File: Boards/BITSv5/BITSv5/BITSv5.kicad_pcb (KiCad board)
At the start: 4 copper layers, 47 x 45 mm, 104 parts, among them J1 Conn_01x10_Pin, J2 USB_C_Receptacle_USB2.0, J3 SOICbite, Q1 Q_NMOS_GSD, SW1 SW_Push, SW3 SLIDE, U1 MCU_RaspberryPi_RP2040_RP2040, U10 USBLC6-2SC6, U11 MS5607-02BA, U2 W25Q128JVS, U3 MAX-M10S, U4 DRF1262TL, U5 LT8653SIV-PBF, U6 TPS2121RUXR, U7 MAX6747KA29+T, U8 LT6703CDC-3, U9 TVS1800DRVR, Y1 12MHz

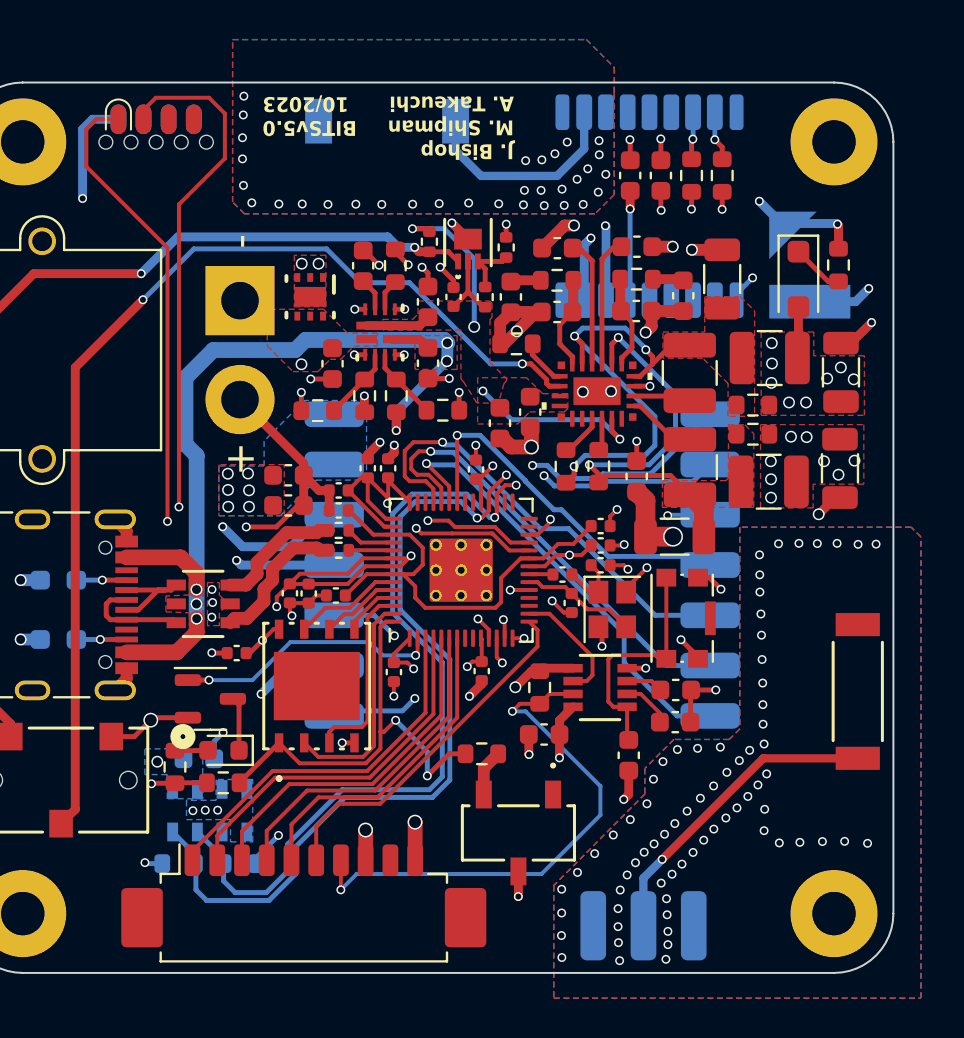
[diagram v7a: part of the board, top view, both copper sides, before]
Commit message: changed BITSv5 antennas to ufl, added TIMEPULSE and EXTINT GPIOs, and exposed GPIO UART over header
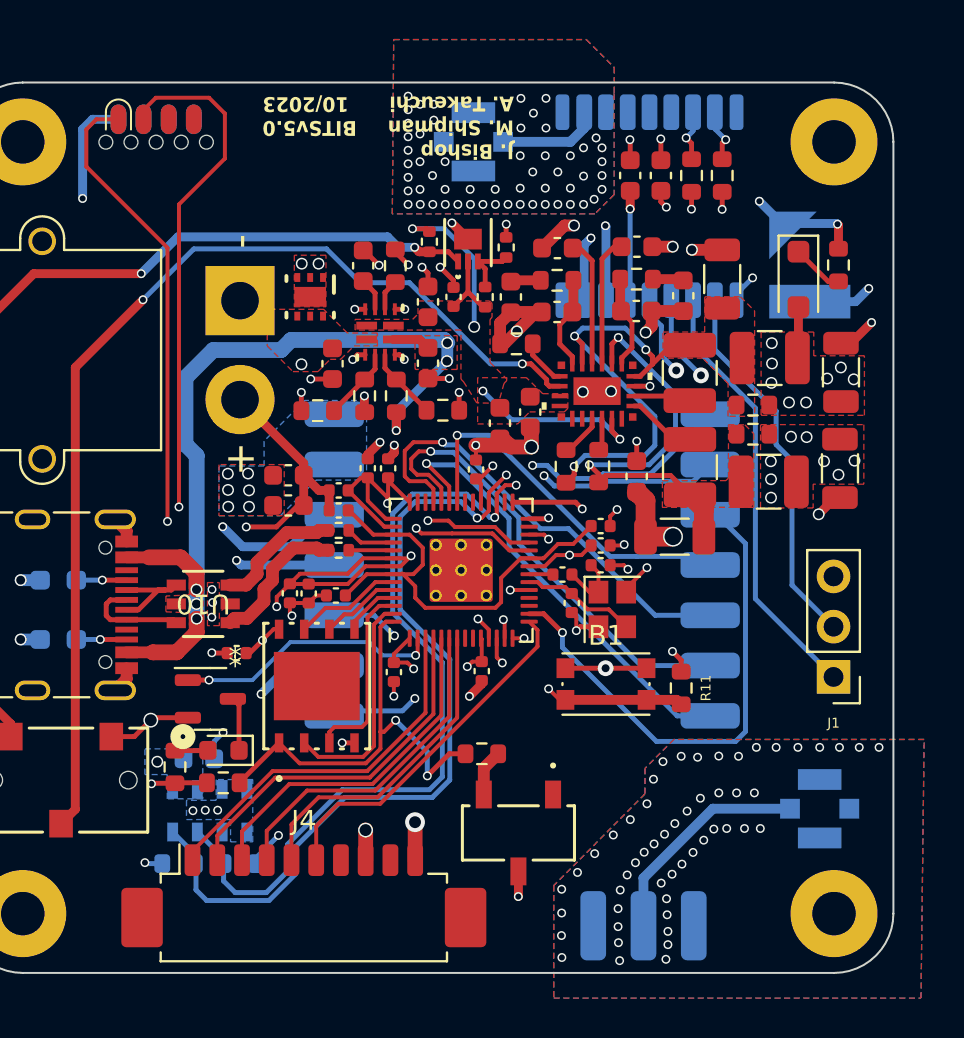
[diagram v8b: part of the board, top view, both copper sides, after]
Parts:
- removed AE1: Antenna, BITSv5:ANT_1575AT_JOT-M
- removed AE2: Antenna, BITSv5:ANT_0915AT43A0026E_JOT
- removed C30, C42: 100nF, Capacitor_SMD:C_0603_1608Metric
- removed C41: 1uF, Capacitor_SMD:C_0603_1608Metric
- removed C43: 200nF, Capacitor_SMD:C_0603_1608Metric
- removed SW1: SW_Push, Button_Switch_SMD:SW_Push_1P1T-SH_NO_CK_KMR2xxG
- removed U7: MAX6747KA29+T, BITSv5:21-0078H_MXM
- added B1: KMR2, Button_Switch_SMD:SW_Push_1P1T_NO_CK_KMR2, F.Cu at (137.7, 72.6)
- added J4: Conn_01x10_Pin, Connector_Molex:Molex_PicoBlade_53261-1071_1x10-1MP_P1.25mm_Horizontal, F.Cu at (122.4, 83.9)
- added J5: U.FL, Connector_Coaxial:U.FL_Molex_MCRF_73412-0110_Vertical, B.Cu at (131.0, 45.2)
- added J6: U.FL, Connector_Coaxial:U.FL_Molex_MCRF_73412-0110_Vertical, B.Cu at (148.5, 78.9)
- C20: value 100uF -> 47uF
- J1: value Conn_01x10_Pin -> Conn_01x03_Pin; footprint Connector_Molex:Molex_PicoBlade_53261-1071_1x10-1MP_P1.25mm_Horizontal -> Connector_PinHeader_2.54mm:PinHeader_1x03_P2.54mm_Vertical
- R11: value 100K -> 10k
- R6, R9: value 10K -> DNF
- moved J1 29.2 mm to (149.2, 72.2), turned to 180 degrees
- moved R11 7.15 mm to (141.5, 72.8)
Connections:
- J1 pad 1: /IRIDIUM_RXD -> Net-(J1-Pin_1)
- J1 pad 2: /IRIDIUM_CTS -> Net-(J1-Pin_2)
- J1 pad 3: /IRIDIUM_RTS -> GND
- R11 pad 2: /RESET -> Net-(U1-RUN)
- U1 pad 16: /WATCHDOG -> /RDIO_RST
- U1 pad 26: /RESET -> Net-(U1-RUN)
- U1 pad 28: unconnected-(U1-GPIO17-Pad28) -> /EXTINT
- U1 pad 29: unconnected-(U1-GPIO18-Pad29) -> /TIMEPULSE
- U3 pad 2: unconnected-(U3-TXD-Pad2) -> Net-(J1-Pin_2)
- U3 pad 3: unconnected-(U3-RXD-Pad3) -> Net-(J1-Pin_1)
- U3 pad 4: unconnected-(U3-TIMEPULSE-Pad4) -> /TIMEPULSE
- U3 pad 5: unconnected-(U3-EXTINT-Pad5) -> /EXTINT
- U4 pad 10: /RESET -> /RDIO_RST
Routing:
- net /RESET: track 47.2 -> 0.00 mm, vias 4 -> 0
- net /RDIO_RST: track 0.00 -> 26.1 mm, vias 0 -> 1
- net Net-(J1-Pin_1): track 0.00 -> 22.0 mm
- net Net-(J1-Pin_2): track 0.00 -> 19.0 mm
- net /TIMEPULSE: track 0.00 -> 17.9 mm, vias 0 -> 2
- net /EXTINT: track 0.00 -> 16.1 mm, vias 0 -> 2
- net Net-(U1-RUN): track 0.00 -> 15.7 mm, vias 0 -> 2
- net Net-(U7-*MR): track 12.1 -> 0.00 mm
- net /SDA: track 70.9 -> 64.1 mm
- net /WATCHDOG: track 6.14 -> 0.00 mm
- net Net-(J5-In): track 10.9 -> 5.19 mm
- net +3V3: track 73.0 -> 68.0 mm, vias 27 -> 26
- net Net-(J6-In): track 15.7 -> 11.3 mm, vias 1 -> 0
- net VCC: track 24.3 -> 21.0 mm
- net GND: track 116.0 -> 112.9 mm, vias 171 -> 170
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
